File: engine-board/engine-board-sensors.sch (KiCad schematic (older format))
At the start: 14 parts, among them J201 Reservoir Pressure Sensor, J202 Bladder Pressure Sensor, J203 HMC6343 COMPASS, J204 QWIIC 1, J205 QWIIC 2, J206 Leak Sensor, J207 BME260 Sensor, J208 RV1805 Clock, U202 BN0055 IMU

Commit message: pcb parts done, footprints updated, ready for routing
pre-routing step..
- finalized footprints
- verified layout, size, mounting holes (1.75" apart)
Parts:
- removed TP201: raw leak, TestPoint:TestPoint_THTPad_3.0x3.0mm_Drill1.5mm, symbol Connector:TestPoint
- removed TP202: leak3v3, TestPoint:TestPoint_THTPad_3.0x3.0mm_Drill1.5mm, symbol Connector:TestPoint
- added TP201: TP_RawLeak, TestPoint:TestPoint_Loop_D2.60mm_Drill1.6mm_Beaded, symbol engine-board-eagle-import:TEST-POINTTP_15TH_THRU
- added TP202: TP_LeakSense, TestPoint:TestPoint_Loop_D2.60mm_Drill1.6mm_Beaded, symbol engine-board-eagle-import:TEST-POINTTP_15TH_THRU
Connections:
- wire segments 55 -> 56
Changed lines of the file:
@@
 $EndComp
-Wire Wire Line
-	8700 1150 8800 1150
 Wire Wire Line
 	9400 1150 9500 1150
@@
 Wire Wire Line
 	9500 1150 9550 1150
-$Comp
-L Connector:TestPoint TP?
-U 1 1 61A5B5F5
-P 8800 1150
-AR Path="/61A5B5F5" Ref="TP?"  Part="1"
-AR Path="/618F9F5D/61A5B5F5" Ref="TP201"  Part="1"
-F 0 "TP201" H 8858 1268 50  0000 L CNN
-F 1 "raw leak" H 8858 1177 50  0000 L CNN
-F 2 "TestPoint:TestPoint_THTPad_3.0x3.0mm_Drill1.5mm" H 9000 1150 50  0001 C CNN
-F 3 "~" H 9000 1150 50  0001 C CNN
-F 4 "https://www.digikey.com/en/products/detail/keystone-electronics/1041/315158" H 8800 1150 50  0001 C CNN "Link"
-F 5 "Keystone" H 8800 1150 50  0001 C CNN "MANUFACTURER"
-F 6 "1041" H 8800 1150 50  0001 C CNN "MPN"
-F 7 "0.30" H 8800 1150 50  0001 C CNN "Price"
-	1    8800 1150
-	1    0    0    -1
-$EndComp
-Connection ~ 8800 1150
-Wire Wire Line
-	8800 1150 9200 1150
-$Comp
-L Connector:TestPoint TP?
-U 1 1 61A5B5FD
-P 9500 1650
-AR Path="/61A5B5FD" Ref="TP?"  Part="1"
-AR Path="/618F9F5D/61A5B5FD" Ref="TP202"  Part="1"
-F 0 "TP202" H 9558 1768 50  0000 L CNN
-F 1 "leak3v3" H 9558 1677 50  0000 L CNN
-F 2 "TestPoint:TestPoint_THTPad_3.0x3.0mm_Drill1.5mm" H 9700 1650 50  0001 C CNN
-F 3 "~" H 9700 1650 50  0001 C CNN
-F 4 "https://www.digikey.com/en/products/detail/keystone-electronics/1041/315158" H 9500 1650 50  0001 C CNN "Link"
-F 5 "Keystone" H 9500 1650 50  0001 C CNN "MANUFACTURER"
-F 6 "1041" H 9500 1650 50  0001 C CNN "MPN"
-F 7 "0.30" H 9500 1650 50  0001 C CNN "Price"
-	1    9500 1650
-	1    0    0    -1
-$EndComp
 Wire Wire Line
 	9250 1650 9500 1650
@@
 Wire Wire Line
 	7250 4400 7550 4400
+$Comp
+L engine-board-eagle-import:TEST-POINTTP_15TH_THRU TP?
+U 1 1 61D1F9DE
+P 9500 1650
+AR Path="/61D1F9DE" Ref="TP?"  Part="1"
+AR Path="/618F9F5D/61D1F9DE" Ref="TP202"  Part="1"
+F 0 "TP202" H 9544 1890 70  0000 C CNN
+F 1 "TP_LeakSense" H 9544 1769 70  0000 C CNN
+F 2 "TestPoint:TestPoint_Loop_D2.60mm_Drill1.6mm_Beaded" H 9500 1650 50  0001 C CNN
+F 3 "https://www.keyelco.com/userAssets/file/M65p64.pdf" H 9500 1650 50  0001 C CNN
+F 4 "0.23" H 9500 1650 50  0001 C CNN "Price"
+F 5 "680" H 9500 1650 50  0001 C CNN "MFN"
+F 6 "https://www.digikey.com/en/products/detail/keystone-electronics/680/316581" H 9500 1650 50  0001 C CNN "Link"
+	1    9500 1650
+	1    0    0    -1
+$EndComp
+Wire Wire Line
+	8700 1150 8950 1150
+$Comp
+L engine-board-eagle-import:TEST-POINTTP_15TH_THRU TP?
+U 1 1 61D26F9C
+P 8950 850
+AR Path="/61D26F9C" Ref="TP?"  Part="1"
+AR Path="/618F9F5D/61D26F9C" Ref="TP201"  Part="1"
+F 0 "TP201" H 8994 1090 70  0000 C CNN
+F 1 "TP_RawLeak" H 8994 969 70  0000 C CNN
+F 2 "TestPoint:TestPoint_Loop_D2.60mm_Drill1.6mm_Beaded" H 8950 850 50  0001 C CNN
+F 3 "https://www.keyelco.com/userAssets/file/M65p64.pdf" H 8950 850 50  0001 C CNN
+F 4 "0.23" H 8950 850 50  0001 C CNN "Price"
+F 5 "680" H 8950 850 50  0001 C CNN "MFN"
+F 6 "https://www.digikey.com/en/products/detail/keystone-electronics/680/316581" H 8950 850 50  0001 C CNN "Link"
+	1    8950 850
+	1    0    0    -1
+$EndComp
+Wire Wire Line
+	8950 850  8950 1150
+Connection ~ 8950 1150
+Wire Wire Line
+	8950 1150 9200 1150
 $EndSCHEMATC

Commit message: shortend pcb, ready to route
ready to route, shortend pcb, layout complete
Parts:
- removed TP201: TP_RawLeak, TestPoint:TestPoint_Loop_D2.60mm_Drill1.6mm_Beaded, symbol engine-board-eagle-import:TEST-POINTTP_15TH_THRU
- removed TP202: TP_LeakSense, TestPoint:TestPoint_Loop_D2.60mm_Drill1.6mm_Beaded, symbol engine-board-eagle-import:TEST-POINTTP_15TH_THRU
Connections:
- wire segments 56 -> 54
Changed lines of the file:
@@
 Wire Wire Line
 	7250 4400 7550 4400
-$Comp
-L engine-board-eagle-import:TEST-POINTTP_15TH_THRU TP?
-U 1 1 61D1F9DE
-P 9500 1650
-AR Path="/61D1F9DE" Ref="TP?"  Part="1"
-AR Path="/618F9F5D/61D1F9DE" Ref="TP202"  Part="1"
-F 0 "TP202" H 9544 1890 70  0000 C CNN
-F 1 "TP_LeakSense" H 9544 1769 70  0000 C CNN
-F 2 "TestPoint:TestPoint_Loop_D2.60mm_Drill1.6mm_Beaded" H 9500 1650 50  0001 C CNN
-F 3 "https://www.keyelco.com/userAssets/file/M65p64.pdf" H 9500 1650 50  0001 C CNN
-F 4 "0.23" H 9500 1650 50  0001 C CNN "Price"
-F 5 "680" H 9500 1650 50  0001 C CNN "MFN"
-F 6 "https://www.digikey.com/en/products/detail/keystone-electronics/680/316581" H 9500 1650 50  0001 C CNN "Link"
-	1    9500 1650
-	1    0    0    -1
-$EndComp
 Wire Wire Line
-	8700 1150 8950 1150
-$Comp
-L engine-board-eagle-import:TEST-POINTTP_15TH_THRU TP?
-U 1 1 61D26F9C
-P 8950 850
-AR Path="/61D26F9C" Ref="TP?"  Part="1"
-AR Path="/618F9F5D/61D26F9C" Ref="TP201"  Part="1"
-F 0 "TP201" H 8994 1090 70  0000 C CNN
-F 1 "TP_RawLeak" H 8994 969 70  0000 C CNN
-F 2 "TestPoint:TestPoint_Loop_D2.60mm_Drill1.6mm_Beaded" H 8950 850 50  0001 C CNN
-F 3 "https://www.keyelco.com/userAssets/file/M65p64.pdf" H 8950 850 50  0001 C CNN
-F 4 "0.23" H 8950 850 50  0001 C CNN "Price"
-F 5 "680" H 8950 850 50  0001 C CNN "MFN"
-F 6 "https://www.digikey.com/en/products/detail/keystone-electronics/680/316581" H 8950 850 50  0001 C CNN "Link"
-	1    8950 850
-	1    0    0    -1
-$EndComp
-Wire Wire Line
-	8950 850  8950 1150
-Connection ~ 8950 1150
-Wire Wire Line
-	8950 1150 9200 1150
+	8700 1150 9200 1150
 $EndSCHEMATC

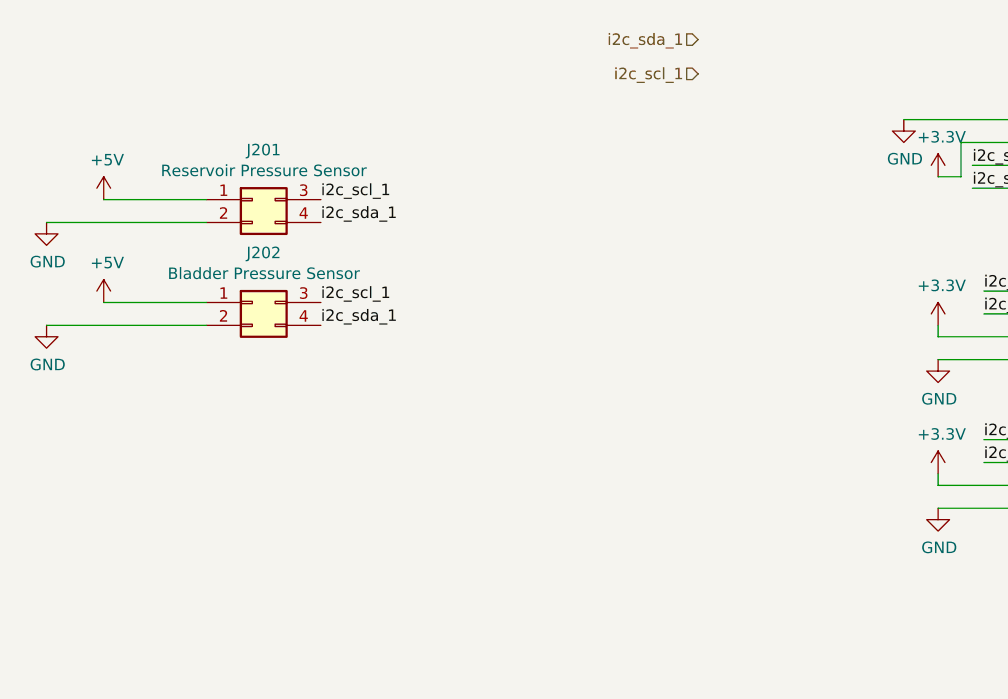
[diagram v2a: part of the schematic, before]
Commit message: ready for layout
- added batt solder tabs
- swapped some terminal blocks with microfit connectors
- shortened board, tightened layout
- tried to space everything out properly
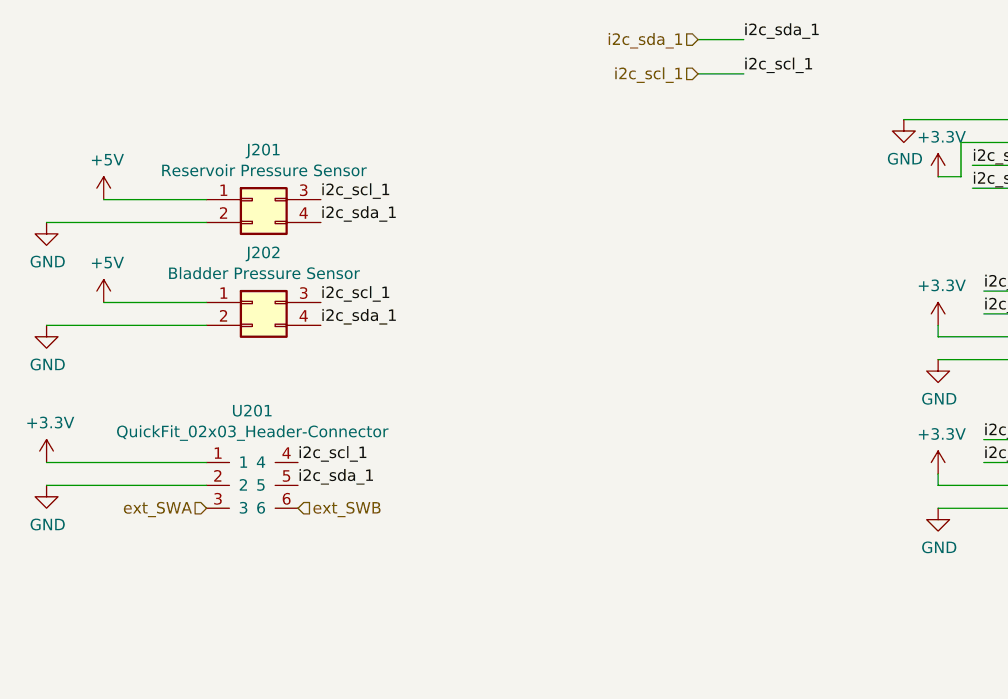
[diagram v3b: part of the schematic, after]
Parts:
- added U201: QuickFit_02x03_Header-Connector, Connector_Molex:Molex_Micro-Fit_3.0_43045-0621_2x03-1MP_P3.00mm_Horizontal, symbol Glider:QuickFit_02x03_Header-Connector
- J201, J202: footprint TerminalBlock_CUI:CUI_TBP01R1W-508-04BE -> Connector_Molex:Molex_Micro-Fit_3.0_43045-0421_2x02-1MP_P3.00mm_Horizontal; Link https://www.digikey.com/en/products/detail/cui-devices/TBP0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 -> https://www.digikey.com/en/products/detail/molex/0430450422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; MANUFACTURER CUI Devices -> Molex; MATE_Link (none) -> https://www.digikey.com/en/products/detail/molex/0430250400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; MATE_MPN (none) -> 430250400; MATE_Price (none) -> 0.48; MPN TBP01R1W-508-04BE -> 0430450422; Price 1.28 -> 2.38
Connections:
- net +3V3: now also U201.1
- net GND: now also U201.2
- net i2c_scl_1: now also U201.4
- net i2c_sda_1: now also U201.5
- new net ext_SWA: U201.3
- new net ext_SWB: U201.6
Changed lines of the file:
@@
 F 0 "J201" H 2100 1667 50  0000 C CNN
 F 1 "Reservoir Pressure Sensor" H 2100 1576 50  0000 C CNN
-F 2 "TerminalBlock_CUI:CUI_TBP01R1W-508-04BE" H 2050 1450 50  0001 C CNN
+F 2 "Connector_Molex:Molex_Micro-Fit_3.0_43045-0421_2x02-1MP_P3.00mm_Horizontal" H 2050 1450 50  0001 C CNN
 F 3 "~" H 2050 1450 50  0001 C CNN
-F 4 "https://www.digikey.com/en/products/detail/cui-devices/TBP01R1W-508-04BE/10238427?WT.z_cid=ref_neda_dkc_buynow_cuidevices&utm_source=ecia&utm_medium=aggregator&utm_campaign=cuidevices" H 2050 1450 50  0001 C CNN "Link"
-F 5 "CUI Devices" H 2050 1450 50  0001 C CNN "MANUFACTURER"
-F 6 "TBP01R1W-508-04BE" H 2050 1450 50  0001 C CNN "MPN"
-F 7 "1.28" H 2050 1450 50  0001 C CNN "Price"
+F 4 "https://www.digikey.com/en/products/detail/molex/0430450422/1635030" H 2050 1450 50  0001 C CNN "Link"
+F 5 "Molex" H 2050 1450 50  0001 C CNN "MANUFACTURER"
+F 6 "0430450422" H 2050 1450 50  0001 C CNN "MPN"
+F 7 "2.38" H 2050 1450 50  0001 C CNN "Price"
+F 8 "430250400" H 2050 1450 50  0001 C CNN "MATE_MPN"
+F 9 "0.48" H 2050 1450 50  0001 C CNN "MATE_Price"
+F 10 "https://www.digikey.com/en/products/detail/molex/0430250400/252497" H 2050 1450 50  0001 C CNN "MATE_Link"
 	1    2050 1450
 	1    0    0    -1
@@
 F 0 "J202" H 2100 2117 50  0000 C CNN
 F 1 "Bladder Pressure Sensor" H 2100 2026 50  0000 C CNN
-F 2 "TerminalBlock_CUI:CUI_TBP01R1W-508-04BE" H 2050 1900 50  0001 C CNN
+F 2 "Connector_Molex:Molex_Micro-Fit_3.0_43045-0421_2x02-1MP_P3.00mm_Horizontal" H 2050 1900 50  0001 C CNN
 F 3 "~" H 2050 1900 50  0001 C CNN
-F 4 "https://www.digikey.com/en/products/detail/cui-devices/TBP01R1W-508-04BE/10238427?WT.z_cid=ref_neda_dkc_buynow_cuidevices&utm_source=ecia&utm_medium=aggregator&utm_campaign=cuidevices" H 2050 1900 50  0001 C CNN "Link"
-F 5 "CUI Devices" H 2050 1900 50  0001 C CNN "MANUFACTURER"
-F 6 "TBP01R1W-508-04BE" H 2050 1900 50  0001 C CNN "MPN"
-F 7 "1.28" H 2050 1900 50  0001 C CNN "Price"
+F 4 "https://www.digikey.com/en/products/detail/molex/0430450422/1635030" H 2050 1900 50  0001 C CNN "Link"
+F 5 "Molex" H 2050 1900 50  0001 C CNN "MANUFACTURER"
+F 6 "0430450422" H 2050 1900 50  0001 C CNN "MPN"
+F 7 "2.38" H 2050 1900 50  0001 C CNN "Price"
+F 8 "430250400" H 2050 1900 50  0001 C CNN "MATE_MPN"
+F 9 "0.48" H 2050 1900 50  0001 C CNN "MATE_Price"
+F 10 "https://www.digikey.com/en/products/detail/molex/0430250400/252497" H 2050 1900 50  0001 C CNN "MATE_Link"
 	1    2050 1900
 	1    0    0    -1
@@
 Wire Wire Line
 	8700 1150 9200 1150
+$Comp
+L power:GND #PWR0114
+U 1 1 61FDFD4D
+P 1150 2700
+F 0 "#PWR0114" H 1150 2450 50  0001 C CNN
+F 1 "GND" H 1155 2527 50  0000 C CNN
+F 2 "" H 1150 2700 50  0001 C CNN
+F 3 "" H 1150 2700 50  0001 C CNN
+	1    1150 2700
+	1    0    0    -1
+$EndComp
+Text Label 2250 2600 0    50   ~ 0
+i2c_scl_1
+Text Label 2250 2700 0    50   ~ 0
+i2c_sda_1
+Wire Wire Line
+	1150 2700 1850 2700
+$Comp
+L power:+3.3V #PWR?
+U 1 1 61FE7BB0
+P 1150 2600
+AR Path="/61FE7BB0" Ref="#PWR?"  Part="1"
+AR Path="/618F9F5D/61FE7BB0" Ref="#PWR0115"  Part="1"
+F 0 "#PWR0115" H 1150 2450 50  0001 C CNN
+F 1 "+3.3V" H 1165 2773 50  0000 C CNN
+F 2 "" H 1150 2600 50  0001 C CNN
+F 3 "" H 1150 2600 50  0001 C CNN
+	1    1150 2600
+	1    0    0    -1
+$EndComp
+Text Label 4200 900  0    50   ~ 0
+i2c_scl_1
+Text Label 4200 750  0    50   ~ 0
+i2c_sda_1
+Wire Wire Line
+	4200 750  4000 750
+Wire Wire Line
+	4200 900  4000 900
+Text HLabel 1850 2800 0    50   Input ~ 0
+ext_SWA
+Text HLabel 2250 2800 2    50   Input ~ 0
+ext_SWB
+$Comp
+L Glider:QuickFit_02x03_Header-Connector U201
+U 1 1 62037C79
+P 2050 2300
+F 0 "U201" H 2050 2225 50  0000 C CNN
+F 1 "QuickFit_02x03_Header-Connector" H 2050 2134 50  0000 C CNN
+F 2 "Connector_Molex:Molex_Micro-Fit_3.0_43045-0621_2x03-1MP_P3.00mm_Horizontal" H 2000 2450 50  0001 C CNN
+F 3 "" H 2000 2450 50  0001 C CNN
+	1    2050 2300
+	1    0    0    -1
+$EndComp
+Wire Wire Line
+	1850 2600 1150 2600
 $EndSCHEMATC

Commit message: ready for routing
- figured out battery input - going with solder strips + sense wires to reduce connector count
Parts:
- added J209: External Pressure Sensor, Connector_Molex:Molex_Micro-Fit_3.0_43045-0421_2x02-1MP_P3.00mm_Horizontal, symbol Connector_Generic:Conn_02x02_Top_Bottom
- U201: symbol Glider:QuickFit_02x03_Header-Connector -> SeaFlight~Glider:QuickFit_02x03_Header-Connector; Link (none) -> https://www.digikey.com/short/4c5hw39j; MPM (none) -> 430450621; Price (none) -> 2.19
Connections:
- wire segments 58 -> 60
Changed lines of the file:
@@
 	1    0    0    -1
 $EndComp
-Text Label 2250 2600 0    50   ~ 0
+Text Label 2300 2600 0    50   ~ 0
 i2c_scl_1
-Text Label 2250 2700 0    50   ~ 0
+Text Label 2300 2700 0    50   ~ 0
 i2c_sda_1
 Wire Wire Line
@@
 Text HLabel 1850 2800 0    50   Input ~ 0
 ext_SWA
-Text HLabel 2250 2800 2    50   Input ~ 0
+Text HLabel 2300 2800 2    50   Input ~ 0
 ext_SWB
 $Comp
-L Glider:QuickFit_02x03_Header-Connector U201
+L SeaFlight~Glider:QuickFit_02x03_Header-Connector U201
 U 1 1 62037C79
-P 2050 2300
-F 0 "U201" H 2050 2225 50  0000 C CNN
-F 1 "QuickFit_02x03_Header-Connector" H 2050 2134 50  0000 C CNN
-F 2 "Connector_Molex:Molex_Micro-Fit_3.0_43045-0621_2x03-1MP_P3.00mm_Horizontal" H 2000 2450 50  0001 C CNN
-F 3 "" H 2000 2450 50  0001 C CNN
-	1    2050 2300
+P 2100 2450
+AR Path="/62037C79" Ref="U201"  Part="1"
+AR Path="/618F9F5D/62037C79" Ref="U201"  Part="1"
+F 0 "U201" H 2100 2375 50  0000 C CNN
+F 1 "QuickFit_02x03_Header-Connector" H 2100 2284 50  0000 C CNN
+F 2 "Connector_Molex:Molex_Micro-Fit_3.0_43045-0621_2x03-1MP_P3.00mm_Horizontal" H 2050 2600 50  0001 C CNN
+F 3 "" H 2050 2600 50  0001 C CNN
+F 4 "https://www.digikey.com/short/4c5hw39j" H 2100 2450 50  0001 C CNN "Link"
+F 5 "430450621" H 2100 2450 50  0001 C CNN "MPM"
+F 6 "2.19" H 2100 2450 50  0001 C CNN "Price"
+	1    2100 2450
 	1    0    0    -1
 $EndComp
 Wire Wire Line
 	1850 2600 1150 2600
+$Comp
+L power:+5V #PWR0219
+U 1 1 62120E88
+P 1500 3500
+F 0 "#PWR0219" H 1500 3350 50  0001 C CNN
+F 1 "+5V" H 1515 3673 50  0000 C CNN
+F 2 "" H 1500 3500 50  0001 C CNN
+F 3 "" H 1500 3500 50  0001 C CNN
+	1    1500 3500
+	1    0    0    -1
+$EndComp
+$Comp
+L power:GND #PWR0213
+U 1 1 62120E8E
+P 1250 3600
+F 0 "#PWR0213" H 1250 3350 50  0001 C CNN
+F 1 "GND" H 1255 3427 50  0000 C CNN
+F 2 "" H 1250 3600 50  0001 C CNN
+F 3 "" H 1250 3600 50  0001 C CNN
+	1    1250 3600
+	1    0    0    -1
+$EndComp
+Text Label 2450 3500 0    50   ~ 0
+i2c_scl_1
+Text Label 2450 3600 0    50   ~ 0
+i2c_sda_1
+Wire Wire Line
+	1500 3500 1950 3500
+Wire Wire Line
+	1250 3600 1950 3600
+$Comp
+L Connector_Generic:Conn_02x02_Top_Bottom J209
+U 1 1 62120E9F
+P 2150 3500
+F 0 "J209" H 2200 3717 50  0000 C CNN
+F 1 "External Pressure Sensor" H 2200 3626 50  0000 C CNN
+F 2 "Connector_Molex:Molex_Micro-Fit_3.0_43045-0421_2x02-1MP_P3.00mm_Horizontal" H 2150 3500 50  0001 C CNN
+F 3 "~" H 2150 3500 50  0001 C CNN
+F 4 "https://www.digikey.com/short/b28q047p" H 2150 3500 50  0001 C CNN "Link"
+F 5 "Molex" H 2150 3500 50  0001 C CNN "MANUFACTURER"
+F 6 "0430450421" H 2150 3500 50  0001 C CNN "MPN"
+F 7 "2.04" H 2150 3500 50  0001 C CNN "Price"
+F 8 "430250400" H 2150 3500 50  0001 C CNN "MATE_MPN"
+F 9 "0.48" H 2150 3500 50  0001 C CNN "MATE_Price"
+F 10 "https://www.digikey.com/en/products/detail/molex/0430250400/252497" H 2150 3500 50  0001 C CNN "MATE_Link"
+F 11 "259" H 2150 3500 50  0001 C CNN "Price2"
+F 12 "https://bluerobotics.com/store/sensors-sonars-cameras/sensors/bar100-sensor-r2-rp/" H 2150 3500 50  0001 C CNN "Link2"
+F 13 "BAR100-SENSOR-R2-RP" H 2150 3500 50  0001 C CNN "MPM2"
+	1    2150 3500
+	1    0    0    -1
+$EndComp
 $EndSCHEMATC

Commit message: Verions 1.0 done + ordered
added routes, submitted order
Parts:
- J201: Price2 (none) -> 0
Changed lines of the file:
@@
 F 9 "0.48" H 2050 1450 50  0001 C CNN "MATE_Price"
 F 10 "https://www.digikey.com/en/products/detail/molex/0430250400/252497" H 2050 1450 50  0001 C CNN "MATE_Link"
+F 11 "0" H 2050 1450 50  0001 C CNN "Price2"
 	1    2050 1450
 	1    0    0    -1
